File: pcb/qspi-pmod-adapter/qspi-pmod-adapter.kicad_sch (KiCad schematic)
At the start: 10 parts, among them J1 PMOD plug, J2 PMOD socket, J3 Tiny QSPI socket, U1 W25Q128JVS

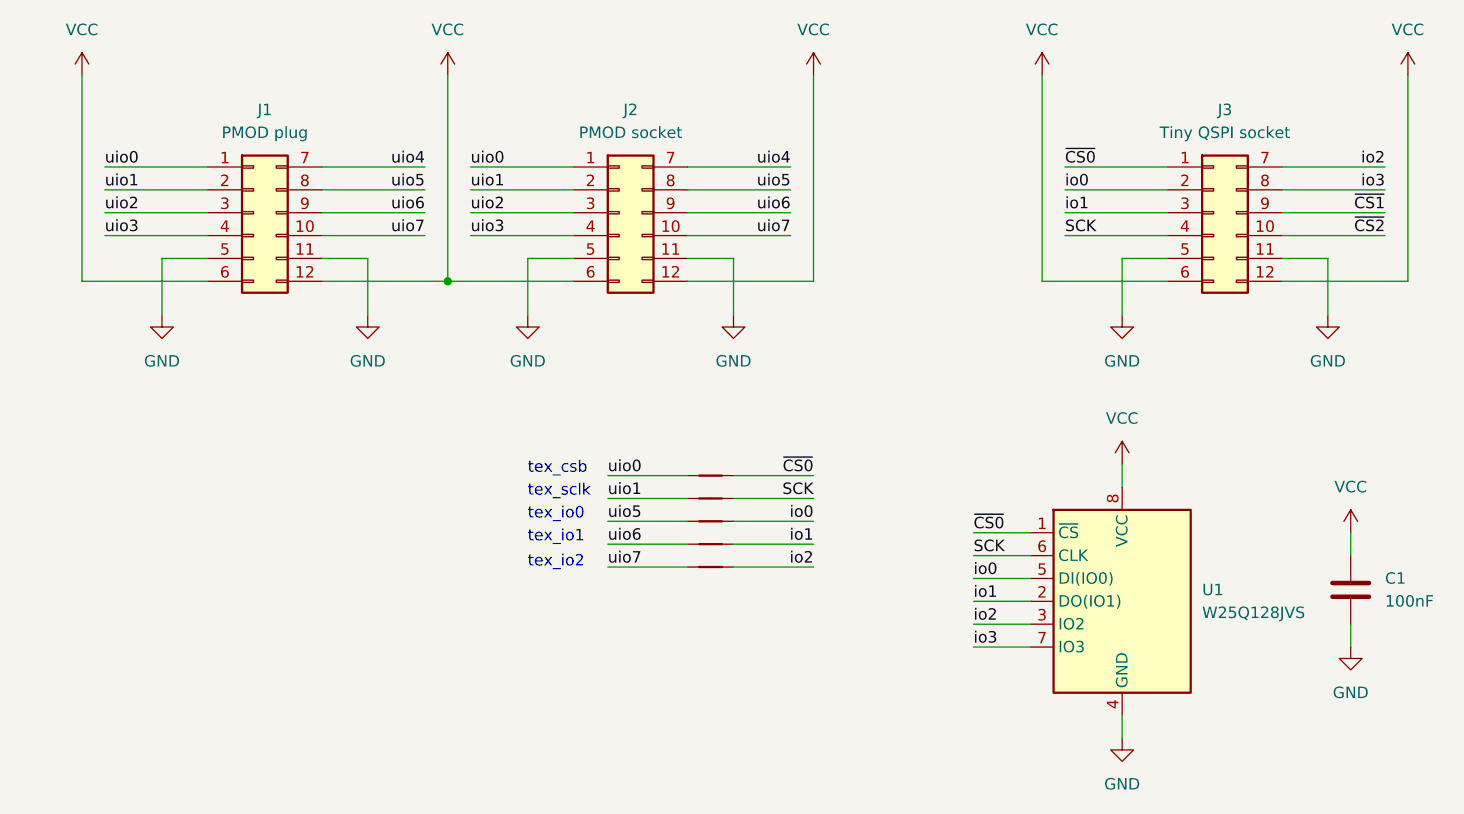
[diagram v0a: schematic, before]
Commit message: tt07b (r1) PCB revision: QSPI adapter dual-plug [no ci]
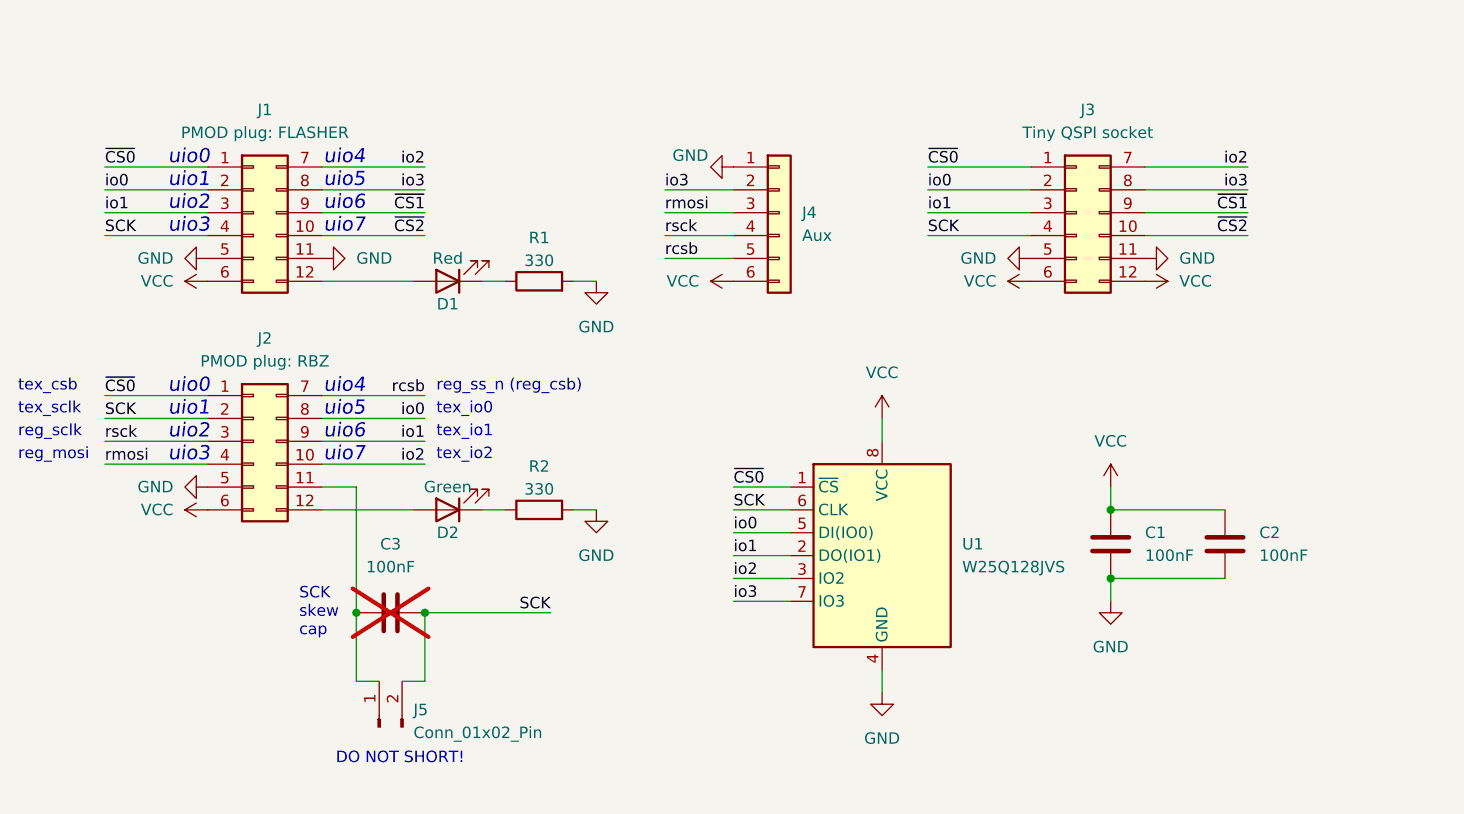
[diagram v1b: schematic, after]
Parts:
- removed NT1, NT2, NT3, NT4, NT5: NetTie_2, NetTie:NetTie-2_SMD_Pad0.5mm, symbol Device:NetTie_2
- added C2, C3: 100nF, Capacitor_SMD:C_0805_2012Metric_Pad1.18x1.45mm_HandSolder, symbol Device:C
- added D1: Red, LED_SMD:LED_0805_2012Metric_Pad1.15x1.40mm_HandSolder, symbol Device:LED
- added D2: Green, LED_SMD:LED_0805_2012Metric_Pad1.15x1.40mm_HandSolder, symbol Device:LED
- added J4: Aux, Connector_PinHeader_2.54mm:PinHeader_1x06_P2.54mm_Vertical, symbol Connector_Generic:Conn_01x06
- added J5: Conn_01x02_Pin, Connector_PinHeader_2.54mm:PinHeader_1x02_P2.54mm_Vertical, symbol Connector:Conn_01x02_Pin
- added R1, R2: 330, Resistor_SMD:R_0805_2012Metric_Pad1.20x1.40mm_HandSolder, symbol Device:R
- J1: value PMOD plug -> PMOD plug: FLASHER
- J2: value PMOD socket -> PMOD plug: RBZ; footprint Anton Kicad Footprints Lib:PinSocket_2x06_P2.54mm_PMODPeriph2B_Vertical -> Anton Kicad Footprints Lib:PinHeader_2x06_P2.54mm_PMODPeriph2B_Clip
- J3: footprint Anton Kicad Footprints Lib:PinSocket_2x06_P2.54mm_PMODPeriph2B_Clip -> Anton Kicad Footprints Lib:PinSocket_2x06_P2.54mm_PMODPeriph2B_Vertical
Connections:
- net uio0 is gone; now on net ~{CS0}: J1.1 (Pin_1), J2.1 (Pin_1)
- net GND: now also C2.2, J4.1 (Pin_1), R1.2, R2.2; no longer J2.11 (Pin_11)
- net SCK: now also J1.4 (Pin_4), J2.2 (Pin_2), C3.2, J5.2 (Pin_2)
- net VCC: now also C2.1, J4.6 (Pin_6); no longer J1.12 (Pin_12), J2.12 (Pin_12)
- net io0: now also J1.2 (Pin_2), J2.8 (Pin_8)
- net io1: now also J1.3 (Pin_3), J2.9 (Pin_9)
- net io2: now also J1.7 (Pin_7), J2.10 (Pin_10)
- net io3: now also J1.8 (Pin_8), J4.2 (Pin_2)
- net ~{CS1}: now also J1.9 (Pin_9)
- net ~{CS2}: now also J1.10 (Pin_10)
- removed net uio1: J1.2 (Pin_2), J2.2 (Pin_2)
- net uio2 renamed rsck
- net rsck: now also J4.4 (Pin_4); no longer J1.3 (Pin_3)
- net uio3 renamed rmosi
- net rmosi: now also J4.3 (Pin_3); no longer J1.4 (Pin_4)
- net uio4 renamed rcsb
- net rcsb: now also J4.5 (Pin_5); no longer J1.7 (Pin_7)
- removed net uio5: J1.8 (Pin_8), J2.8 (Pin_8)
- removed net uio6: J1.9 (Pin_9), J2.9 (Pin_9)
- removed net uio7: J1.10 (Pin_10), J2.10 (Pin_10)
- new net: D2.1 (K), R2.1
- new net: C3.1, J2.11 (Pin_11), J5.1 (Pin_1)
- new net: D1.2 (A), J1.12 (Pin_12)
- new net: D2.2 (A), J2.12 (Pin_12)
- new net: D1.1 (K), R1.1
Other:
- note added: "DO NOT SHORT!"
- note added: "SCK skew cap"
- note added: "reg_mosi"
- note added: "reg_sclk"
- note added: "reg_ss_n (reg_csb)"
- note added: "uio0 uio1 uio2 uio3"
- note added: "uio4 uio5 uio6 uio7"
- moved on the sheet: C1, J3, U1
